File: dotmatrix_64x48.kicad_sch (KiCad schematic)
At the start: 69 parts, among them J1 Conn_01x03_Female, J2 Conn_01x03_Male, J3 Micro_SD_Card, J7 Conn_01x04_Female, P1 CONN_01X06, Q2 Q_NPN_BEC, Q4 Q_NPN_BEC, SW1 SW_PUSH_SMALL_H, SW2 SW_PUSH_SMALL_H, U1 74VHC541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

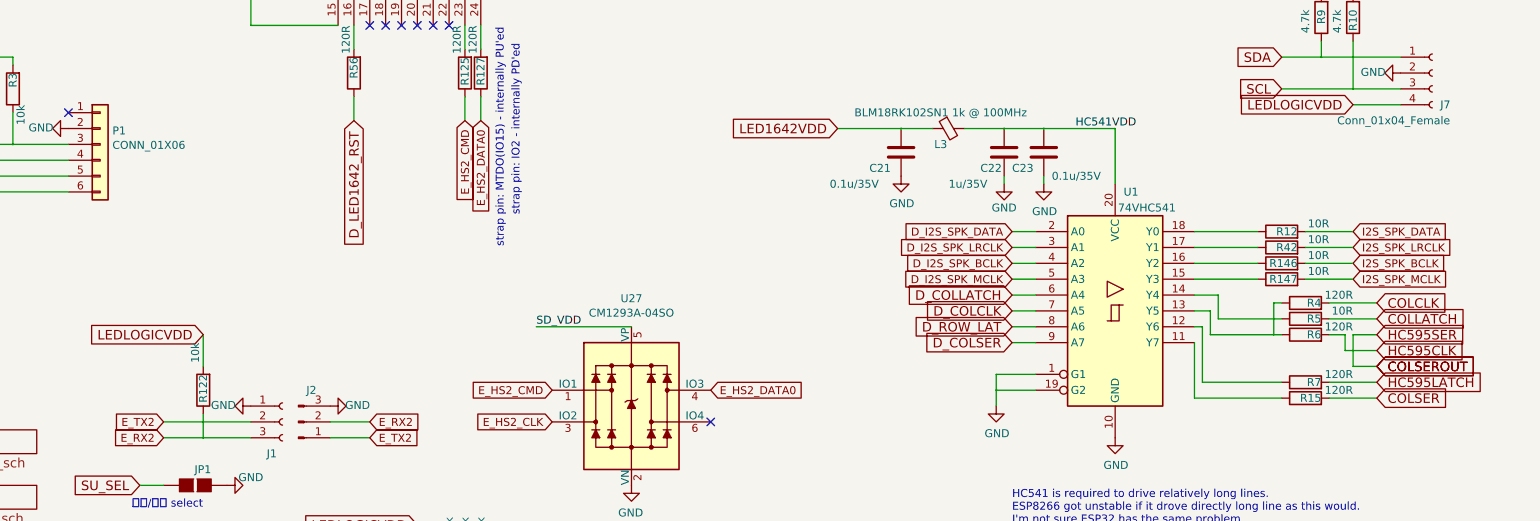
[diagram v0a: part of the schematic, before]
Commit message: Added a schematic comments; I don't know why other files are updated
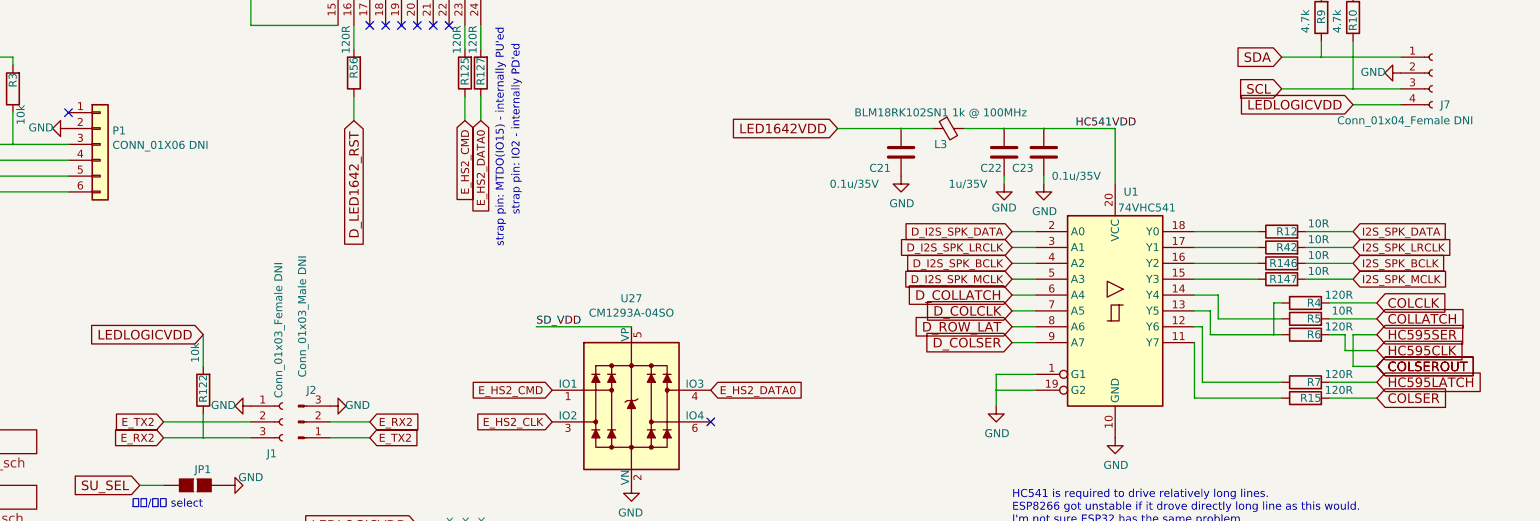
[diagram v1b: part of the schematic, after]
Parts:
- J1: value Conn_01x03_Female -> Conn_01x03_Female DNI
- J2: value Conn_01x03_Male -> Conn_01x03_Male DNI
- J7: value Conn_01x04_Female -> Conn_01x04_Female DNI
- P1: value CONN_01X06 -> CONN_01X06 DNI

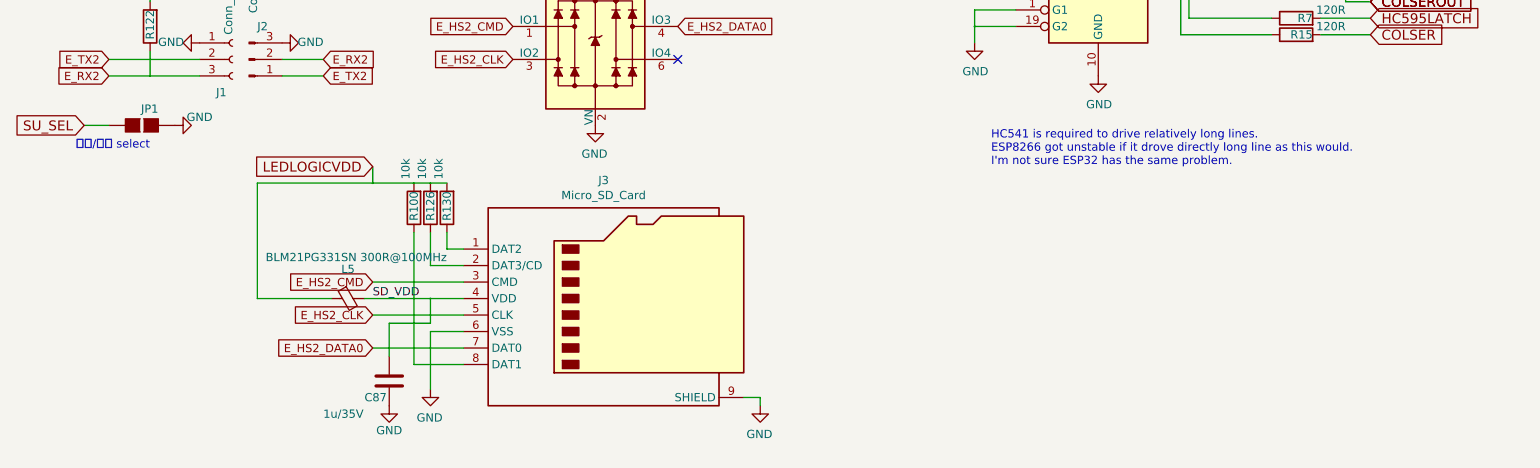
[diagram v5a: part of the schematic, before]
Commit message: Improved SD card VDD line
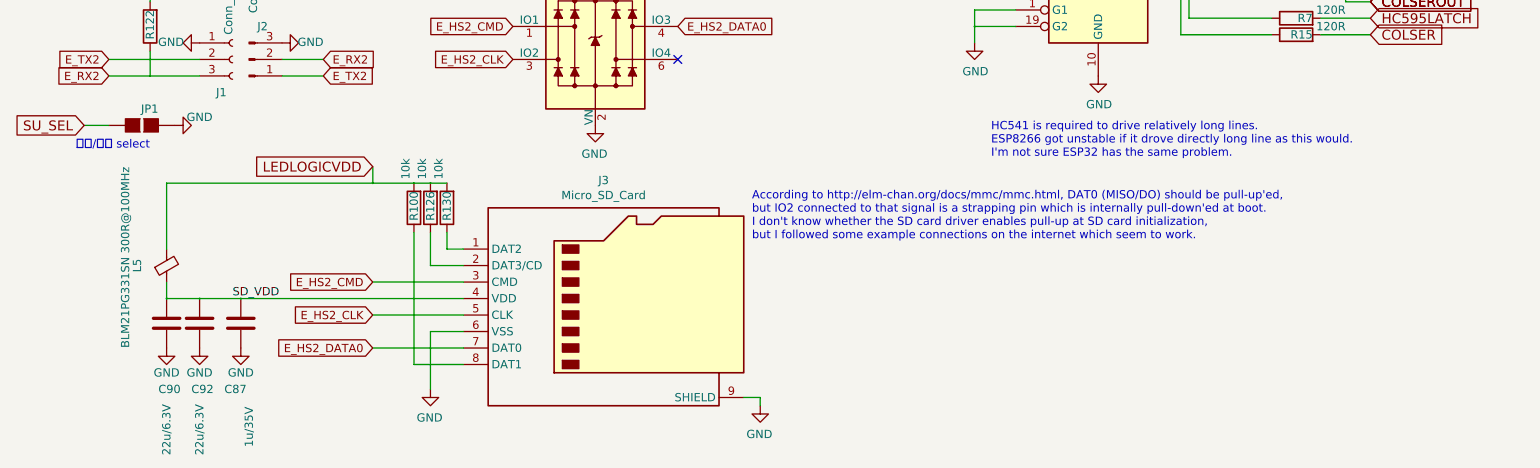
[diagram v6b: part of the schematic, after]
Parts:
- added C90, C92: 22u/6.3V, Capacitor_SMD:C_0603_1608Metric_Pad1.08x0.95mm_HandSolder, symbol dotmatrix_64x48-rescue:C-device
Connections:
- net GND: now also C90.2, C92.2
- net LEDLOGICVDD: now also L5.2; no longer L5.1
- net SD_VDD: now also L5.1, C90.1, C92.1; no longer L5.2
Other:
- note added: "According to http://elm-chan.org/docs/mmc/mmc.html, DAT0 (MISO/DO) should be pull-up'ed, but IO2 connected to that signal is a strapping pin which is internally pull-down'ed at boot. I don't know whether the SD card driver enables pull-up at SD card initialization, but I followed some example connections on the internet which seem to work."
- moved on the sheet: C87, L5
